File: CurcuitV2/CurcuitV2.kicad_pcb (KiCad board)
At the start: 2 copper layers, 40 x 40 mm, 92 parts, among them IC1 AS5600-ASOT, J1 Conn_01x07, J2 Conn_01x03, J3 Conn_01x02, J4 Conn_01x02, Q1 Q_NMOS_DGS, Q2 Q_NMOS_DGS, Q3 Q_NMOS_DGS, Q4 Q_NMOS_DGS, Q5 Q_NMOS_DGS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

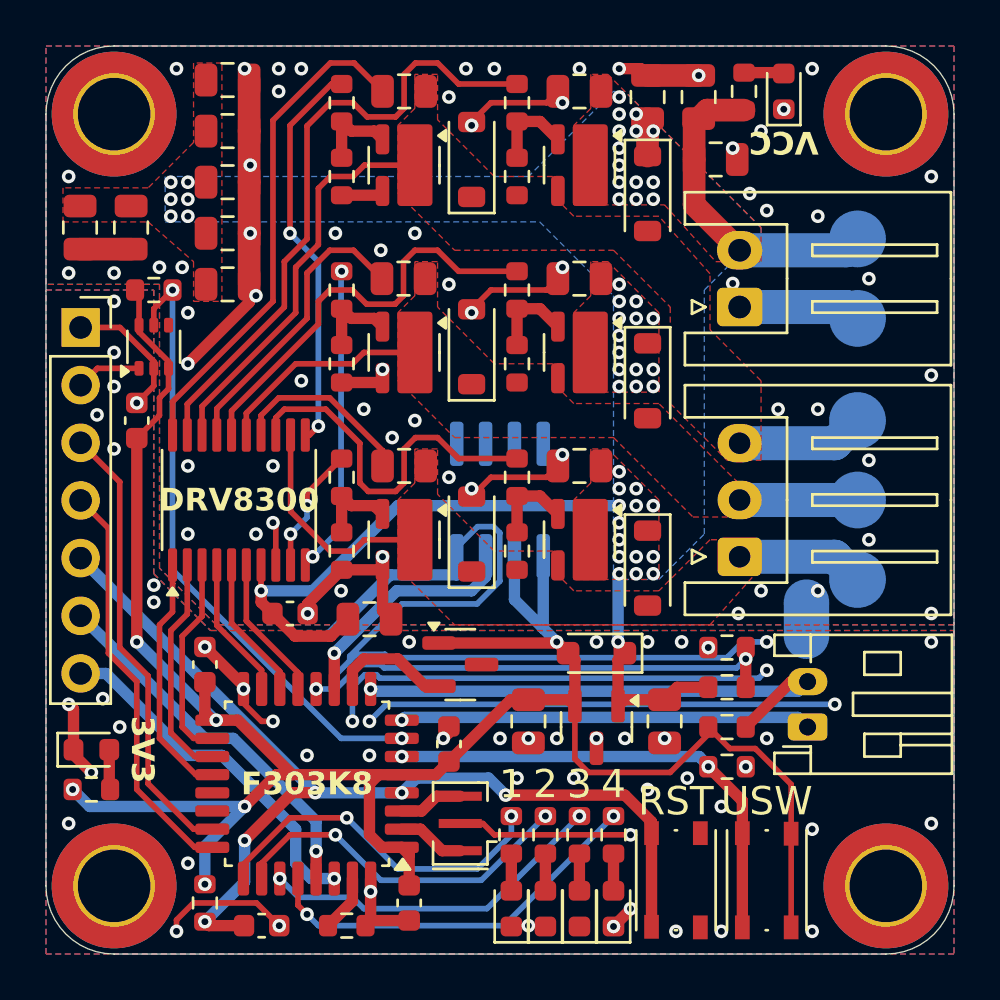
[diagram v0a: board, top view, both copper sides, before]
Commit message: 配線修正
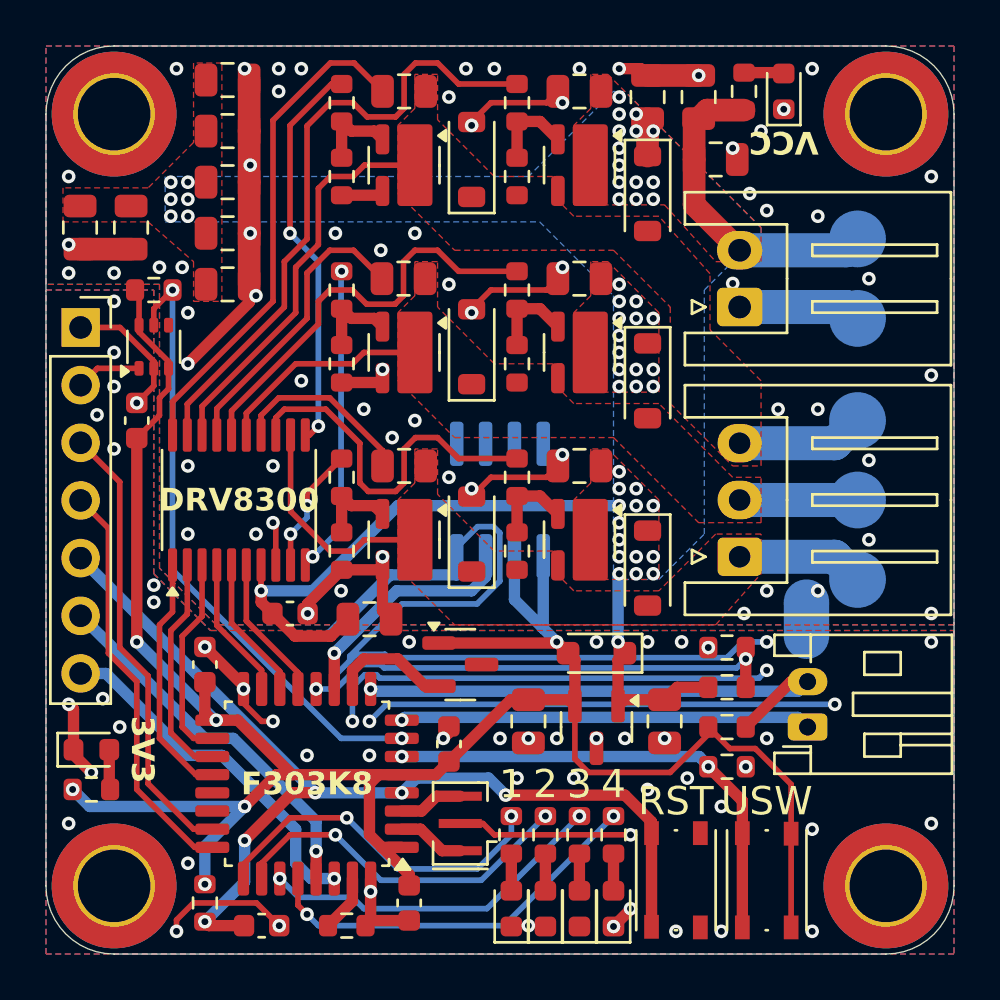
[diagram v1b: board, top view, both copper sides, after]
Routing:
- net GNDA: vias 64 -> 65
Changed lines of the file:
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@@
 	)
 	(segment
-		(start 116 135.625)
-		(end 115.675 135.3)
-		(width 0.5)
-		(layer "F.Cu")
-		(net 2)
-	)
-	(segment
 		(start 105.4 115.1)
 		(end 105 115.5)
@@
 	)
 	(segment
+		(start 116 136.5)
+		(end 114.8 135.3)
+		(width 0.5)
+		(layer "F.Cu")
+		(net 2)
+	)
+	(segment
 		(start 107 128.025)
 		(end 107 129.375)
@@
 	)
 	(segment
+		(start 116 136.975)
+		(end 116 136.5)
+		(width 0.5)
+		(layer "F.Cu")
+		(net 2)
+	)
+	(segment
 		(start 127.499 132.001)
 		(end 123.898678 132.001)
@@
 	)
 	(segment
-		(start 116 136.975)
-		(end 116 135.625)
-		(width 0.5)
-		(layer "F.Cu")
-		(net 2)
-	)
-	(segment
 		(start 104.1 110.925)
 		(end 103.925 110.75)
@@
 	)
 	(via
-		(at 130.5 125)
+		(at 130.75 125)
 		(size 0.6)
 		(drill 0.3)
@@
 	)
 	(via
-		(at 131.5 124)
+		(at 131.75 124)
 		(size 0.6)
 		(drill 0.3)
@@
 	)
 	(via
+		(at 101 108.75)
+		(size 0.6)
+		(drill 0.3)
+		(layers "F.Cu" "B.Cu")
+		(free yes)
+		(net 57)
+	)
+	(via
 		(at 110.25 101)
 		(size 0.6)
@@
 			(pts
 				(xy 116.25 109.5) (xy 116.25 111) (xy 115.5 111.75) (xy 115.5 114.75) (xy 118 117.25) (xy 125 117.25)
-				(xy 128.5 120.75) (xy 130.5 120.75) (xy 130.5 119.25) (xy 127 115.75) (xy 123.25 115.75) (xy 122.75 115.25)
-				(xy 122.75 114) (xy 119.75 114) (xy 117.25 111.5) (xy 117.25 109.5)
+				(xy 128.75 121) (xy 131.5 121) (xy 131.5 119) (xy 130.25 119) (xy 127 115.75) (xy 123.25 115.75)
+				(xy 122.75 115.25) (xy 122.75 114) (xy 119.75 114) (xy 117.25 111.5) (xy 117.25 109.5)
 			)
 		)
@@
 		(polygon
 			(pts
-				(xy 116.25 117.75) (xy 116.25 119.25) (xy 115.5 120) (xy 115.5 123) (xy 118 125.5) (xy 129.25 125.5)
-				(xy 131.25 123.25) (xy 131.25 121.75) (xy 129.25 121.75) (xy 127 124) (xy 123.25 124) (xy 122.75 123.5)
+				(xy 116.25 117.75) (xy 116.25 119.25) (xy 115.5 120) (xy 115.5 123) (xy 118 125.5) (xy 129.5 125.5)
+				(xy 131.5 123.25) (xy 131.5 121.5) (xy 129.5 121.5) (xy 127 124) (xy 123.25 124) (xy 122.75 123.5)
 				(xy 122.75 122.25) (xy 119.75 122.25) (xy 117.25 119.75) (xy 117.25 117.75)
 			)
@@
 			(pts
 				(xy 116.25 101.25) (xy 116.25 102.75) (xy 115.5 103.5) (xy 115.5 106.5) (xy 118 109) (xy 125 109)
-				(xy 127.5 111.5) (xy 127.5 115.75) (xy 130 118.25) (xy 131.5 118.25) (xy 131.5 114.75) (xy 129.25 112.5)
+				(xy 127.5 111.5) (xy 127.5 115.75) (xy 130.25 118.5) (xy 131.5 118.5) (xy 131.5 114.75) (xy 129.25 112.5)
 				(xy 129.25 110.03125) (xy 127 107.5) (xy 123.25 107.5) (xy 122.75 107) (xy 122.75 105.75) (xy 119.75 105.75)
 				(xy 117.25 103.25) (xy 117.25 101.25)

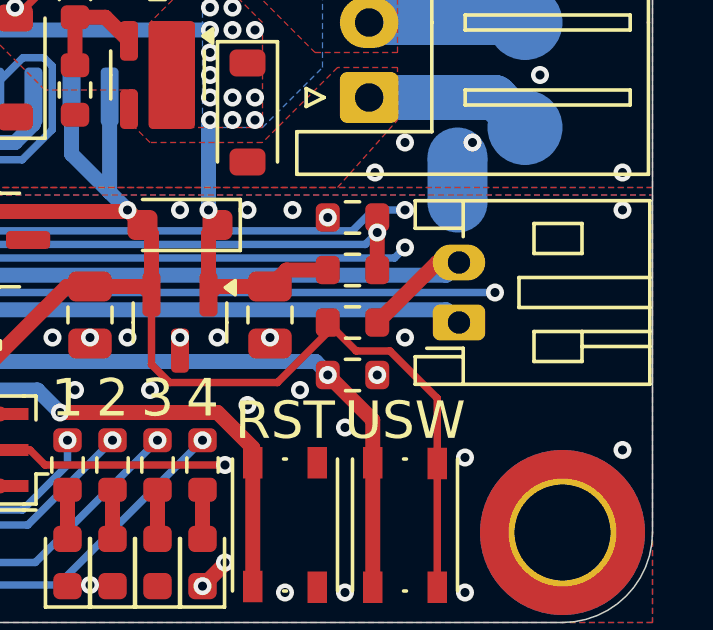
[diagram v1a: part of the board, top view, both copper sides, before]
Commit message: 配線修正
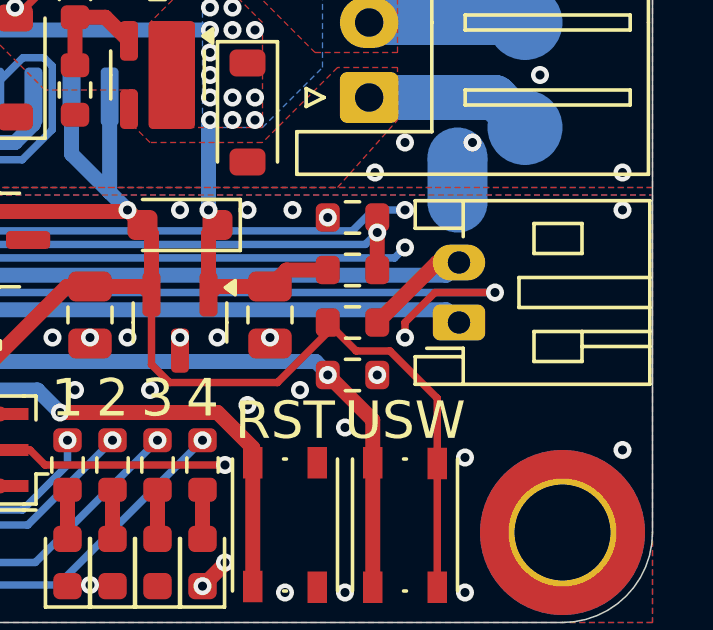
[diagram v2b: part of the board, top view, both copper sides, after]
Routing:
- net GND: track 115.5 -> 119.4 mm
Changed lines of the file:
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@@
+	)
+	(segment
+		(start 131.75 130.5)
+		(end 131.75 130)
+		(width 0.25)
+		(layer "F.Cu")
+		(net 1)
 	)
 	(segment
@@
 	)
 	(segment
+		(start 132.75 129)
+		(end 134.75 129)
+		(width 0.25)
+		(layer "F.Cu")
+		(net 1)
+	)
+	(segment
 		(start 110.275 138.75)
 		(end 109.275 137.75)
@@
 		(layer "F.Cu")
 		(net 1)
+	)
+	(segment
+		(start 131.75 130)
+		(end 132.75 129)
+		(width 0.25)
+		(layer "F.Cu")
+		(net 1)
